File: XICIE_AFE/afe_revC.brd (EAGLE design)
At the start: 100 x 80 mm, 26 parts, among them IC1 LM324N, T1 SFH303

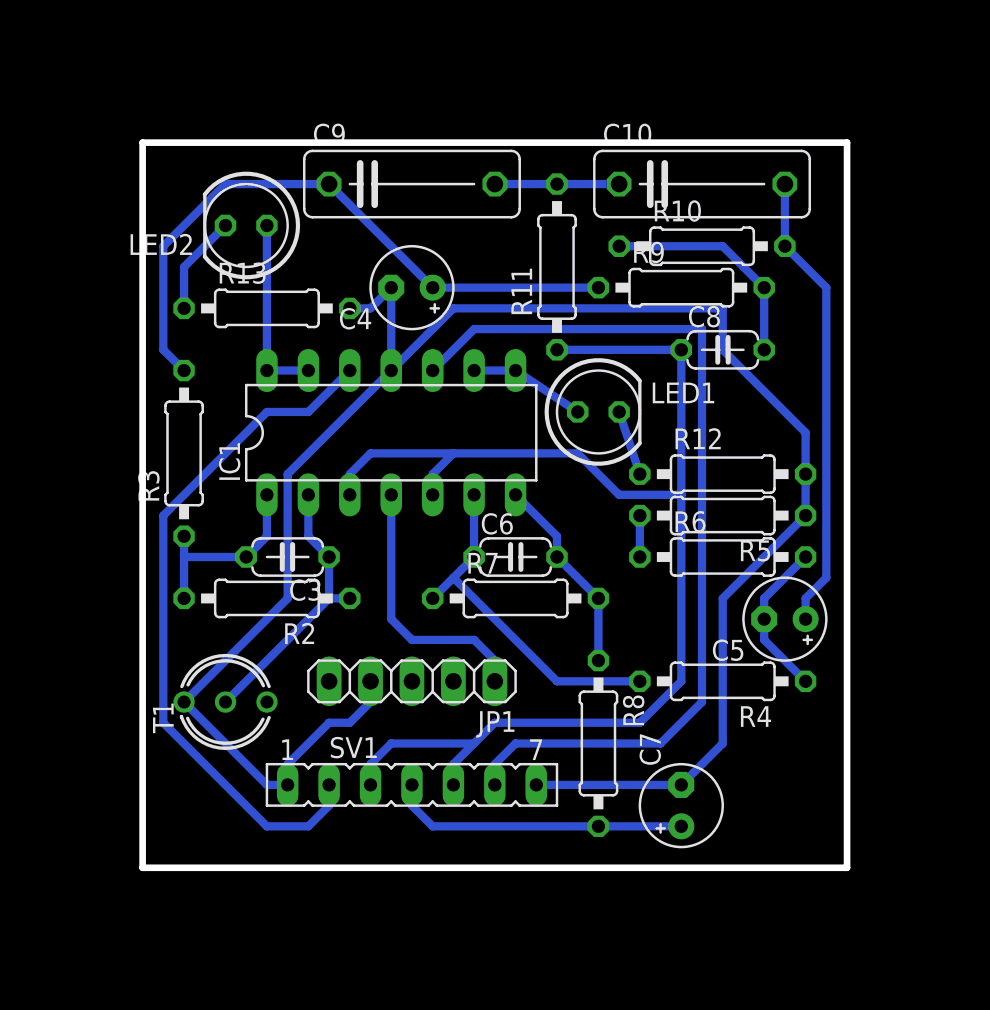
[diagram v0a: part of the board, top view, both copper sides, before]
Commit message: Minor changes in AFE revC and added DISPLAY board
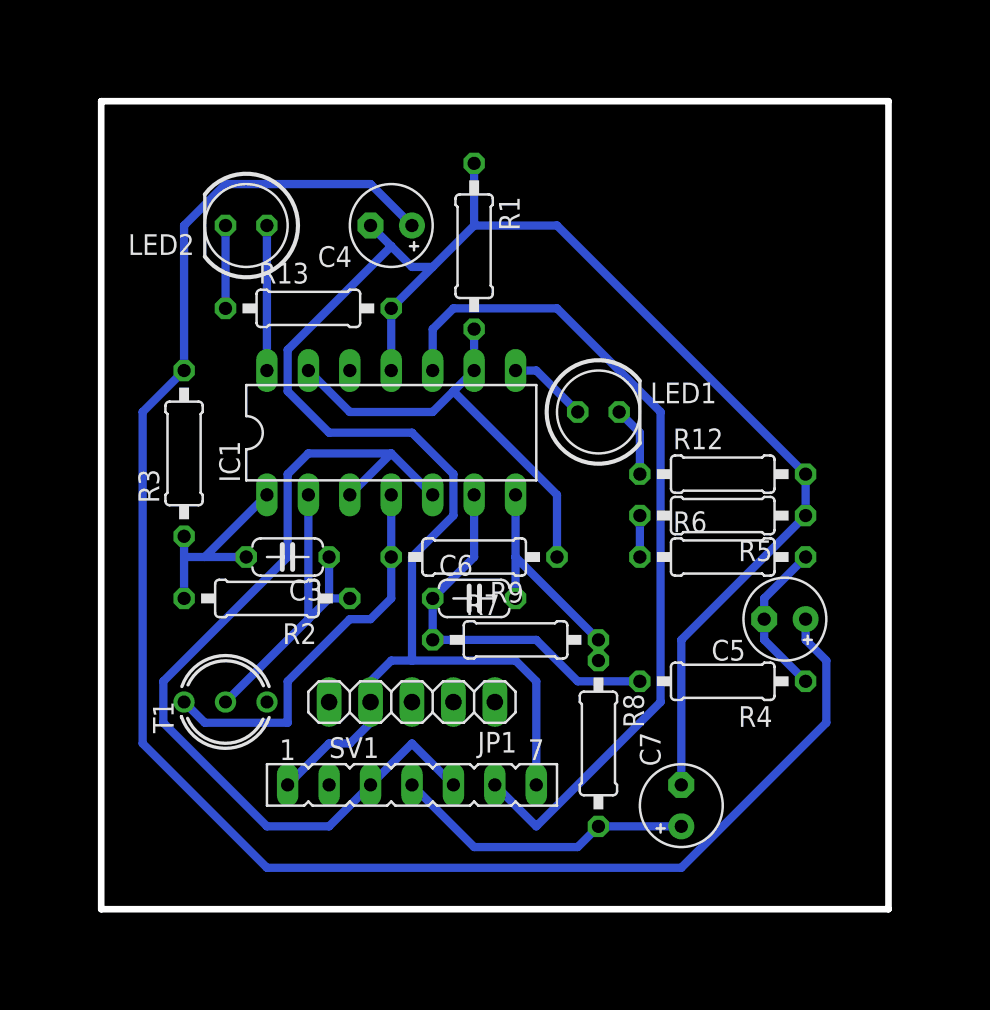
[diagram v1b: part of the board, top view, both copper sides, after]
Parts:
- removed C10, C9: 0.22u, rcl:C102-043X133
- removed C8: 0.1u, rcl:C050-024X044
- removed R10: 33K, rcl:0207/10
- removed R11: 3.3K, rcl:0207/10
- added R1: 150K, rcl:0207/10
- R9: value 33K -> 150K
- moved R9 20.8 mm to (33.0, 34.3), turned to 180 degrees
- moved C4 4.02 mm to (27.9, 54.6)
- moved C6 3.59 mm to (33.0, 31.8)
- moved R13 2.54 mm to (22.9, 49.5)
- moved R7 2.54 mm to (35.6, 29.2)
- moved JP1 1.27 mm to (29.2, 25.4)
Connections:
- removed net N$10: C10.1, C9.2, R11.2
- removed net N$11: IC1.13, IC1.14, LED2.A
- removed net N$8: C8.2, R10.1, R9.2
- removed net N$9: C10.2, C5.+, R10.2
- new net N$15: IC1.8, LED1.A
- new net N$16: IC1.14, LED2.A
- net +5V: now also R9.2, T1.1
- net GND: now also R1.1; no longer T1.1
- net N$12: now also IC1.13, R1.2, R9.1; no longer IC1.8, LED1.A
- net N$3: now also C5.+; no longer C9.1, R9.1
- net VREF: no longer C8.1, R11.1
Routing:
- net N$3: track 39.0 -> 104.5 mm
- net LED2DRIVE: track 42.4 -> 0.00 mm
- net N$9: track 28.2 -> 0.00 mm
- net VREF: track 79.7 -> 56.0 mm
- net N$12: track 7.12 -> 27.6 mm
- net GND: track 116.6 -> 131.5 mm
- net N$8: track 13.8 -> 0.00 mm
- net N$11: track 11.4 -> 0.00 mm
- net N$16: track 0.00 -> 8.89 mm
- net +5V: track 16.3 -> 24.2 mm
- net N$10: track 7.62 -> 0.00 mm
- net N$15: track 0.00 -> 4.86 mm
- net LED1DRIVE: track 56.0 -> 51.8 mm
- net N$2: track 17.1 -> 20.4 mm
- net N$7: track 12.3 -> 14.8 mm
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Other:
- outline, holes or cut-outs redrawn
